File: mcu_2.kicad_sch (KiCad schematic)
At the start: 13 parts, among them U6 STM32G474RETx, Y3 Crystal 24MHz

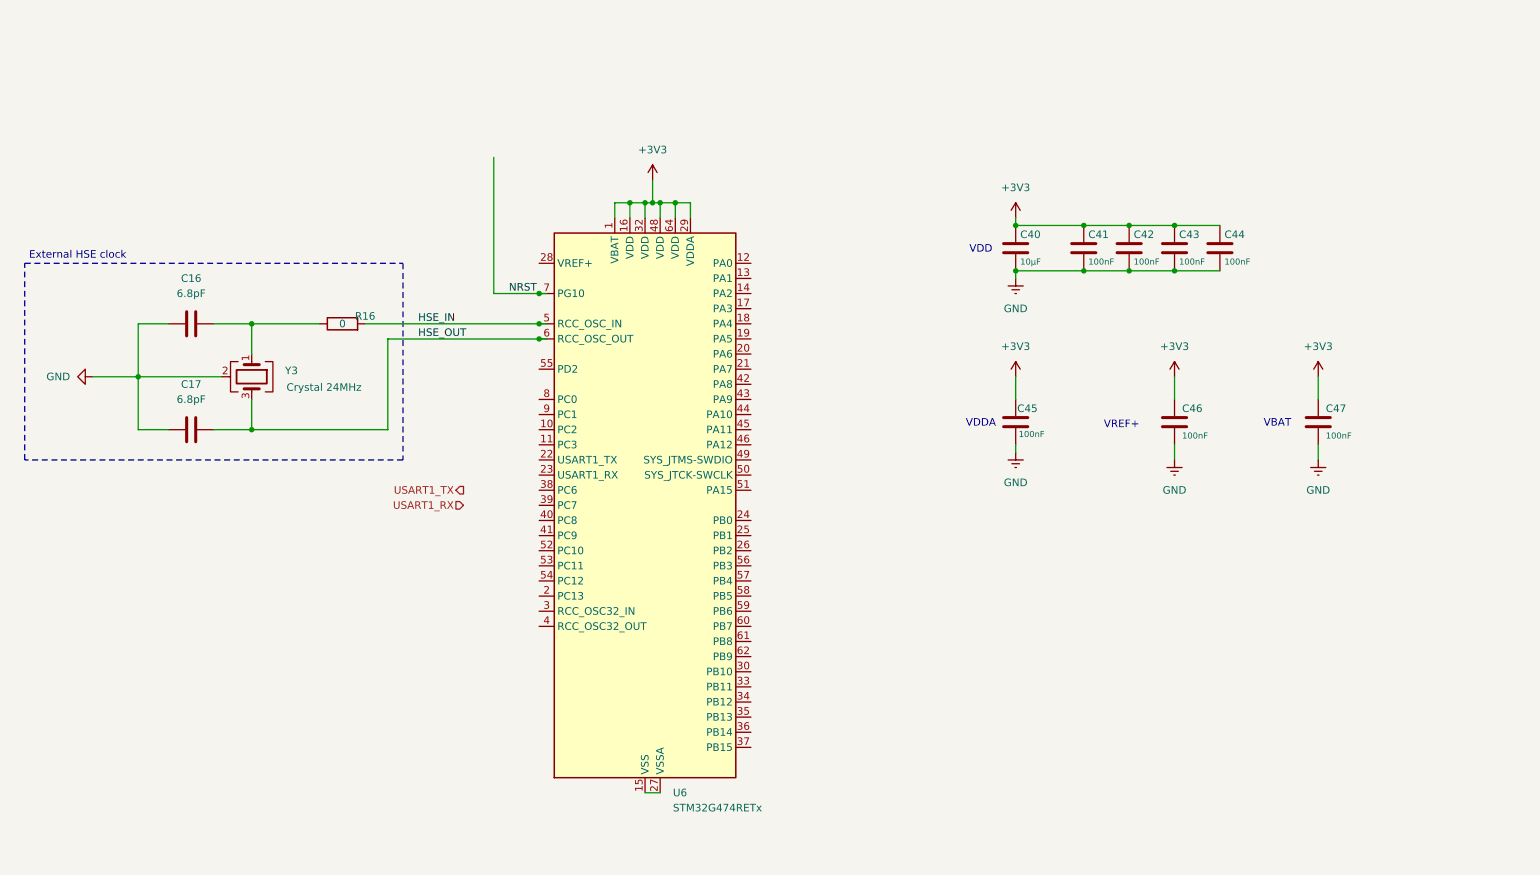
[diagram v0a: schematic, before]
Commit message: Generated scaffold for mcu2 finished brake sense rev2 finished adding second chip to nucleo devboard
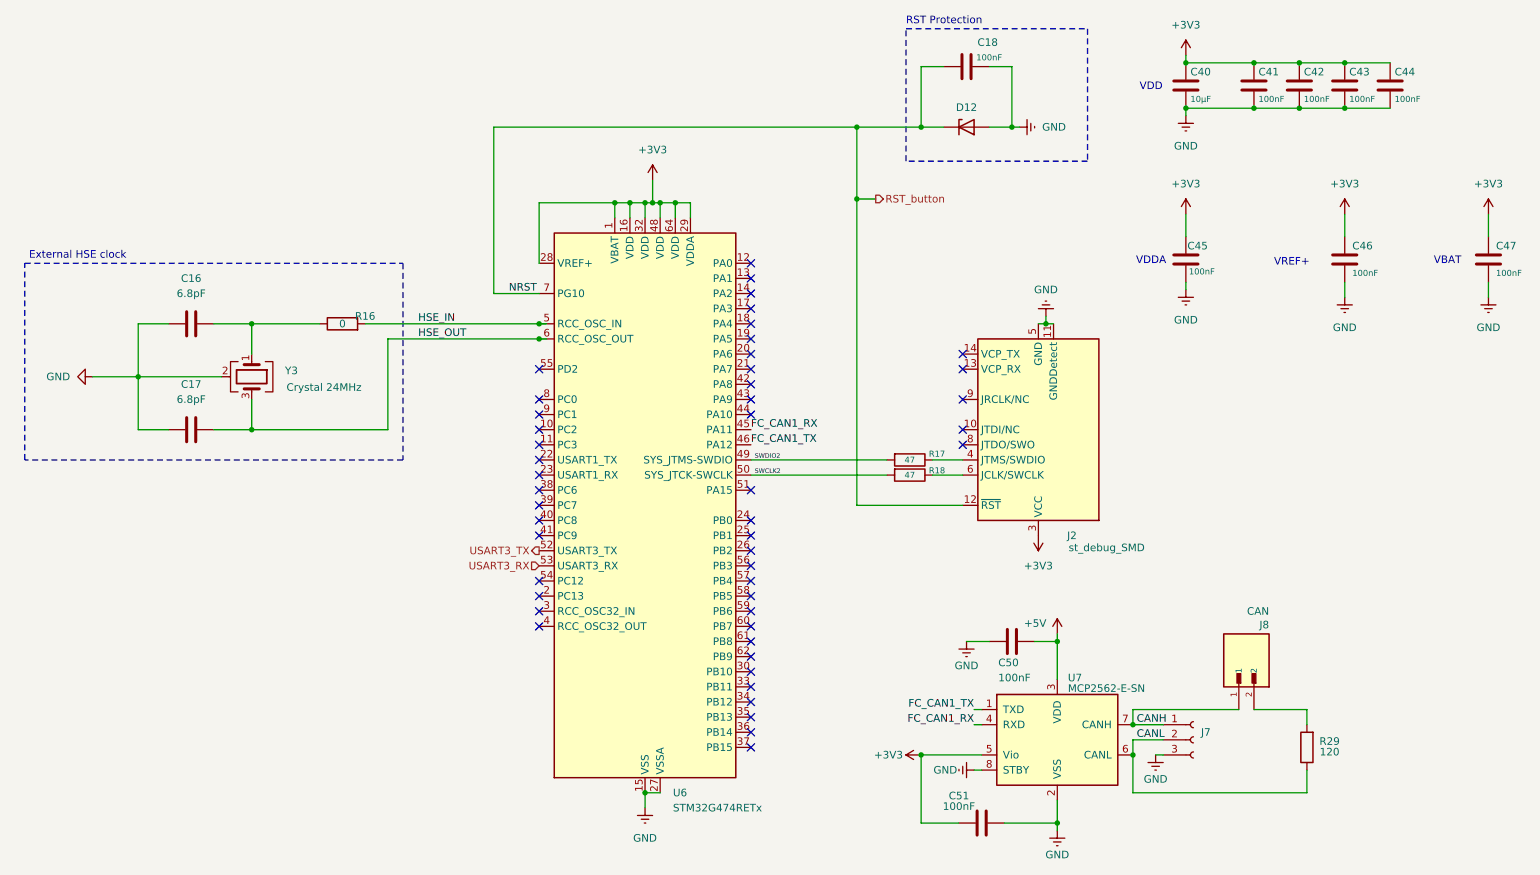
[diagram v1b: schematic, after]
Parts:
- added C18, C50, C51: 100nF, Capacitor_SMD:C_0603_1608Metric, symbol Device:C
- added D12: CDSOD323-T03, Diode_SMD:D_SOD-323, symbol Diode:PESD3V3U1UL
- added J2: st_debug_SMD, tinynav:PinHeader_2x07_P1.27mm_Vertical_SMD, symbol tinynav:st_debug_SMD
- added J7: Conn_01x03_Socket, tinynav:DF3-3P-2DSA, symbol Connector:Conn_01x03_Socket
- added J8: CAN, tinynav:HARWIN_M20-9990246, symbol tinynav:M20-9990246
- added R17, R18: 47, Resistor_SMD:R_0805_2012Metric, symbol Device:R
- added R29: 120, Resistor_SMD:R_0805_2012Metric, symbol Device:R
- added U7: MCP2562-E-SN, Package_SO:SOIC-8_3.9x4.9mm_P1.27mm, symbol Interface_CAN_LIN:MCP2562-E-SN
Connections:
- net +3V3: now also U6.28 (VREF+), C51.1, J2.3 (VCC), U7.5 (Vio)
- net GND: now also U6.15 (VSS), U6.27 (VSSA), U6.31 (VSS), U6.47 (VSS), U6.63 (VSS), C18.2, C50.1, C51.2, D12.2 (A), J2.11 (GNDDetect), J2.5 (GND), J2.7 (GND), J7.3 (Pin_3), U7.2 (VSS), U7.8 (STBY)
- net FC_CAN1_RX: now reaches U6.45 (PA11)
- net FC_CAN1_RX: now also U7.4 (RXD)
- net FC_CAN1_TX: now reaches U6.46 (PA12)
- net FC_CAN1_TX: now also U7.1 (TXD)
- net SWDIO2: now reaches U6.49 (PA13)
- net SWDIO2: now also R17.2
- net SWCLK2: now reaches U6.50 (PA14)
- net SWCLK2: now also R18.2
- net USART3_TX: now reaches U6.52 (PC10)
- net USART3_RX: now reaches U6.53 (PC11)
- net NRST renamed RST_button
- net RST_button: now also C18.1, D12.1 (K), J2.12 (~{RST})
- new net: J8.2, R29.2
- new net: J2.6 (JCLK/SWCLK), R18.1
- new net: J2.4 (JTMS/SWDIO), R17.1
- new net +5V: C50.2, U7.3 (VDD)
- new net CANH: J7.1 (Pin_1), J8.1, U7.7 (CANH)
- new net CANL: J7.2 (Pin_2), R29.1, U7.6 (CANL)
- no-connect marks 0 -> 48
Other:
- note added: "RST Protection"
- moved on the sheet: C40, C41, C42, C43, C44, C45, C46, C47

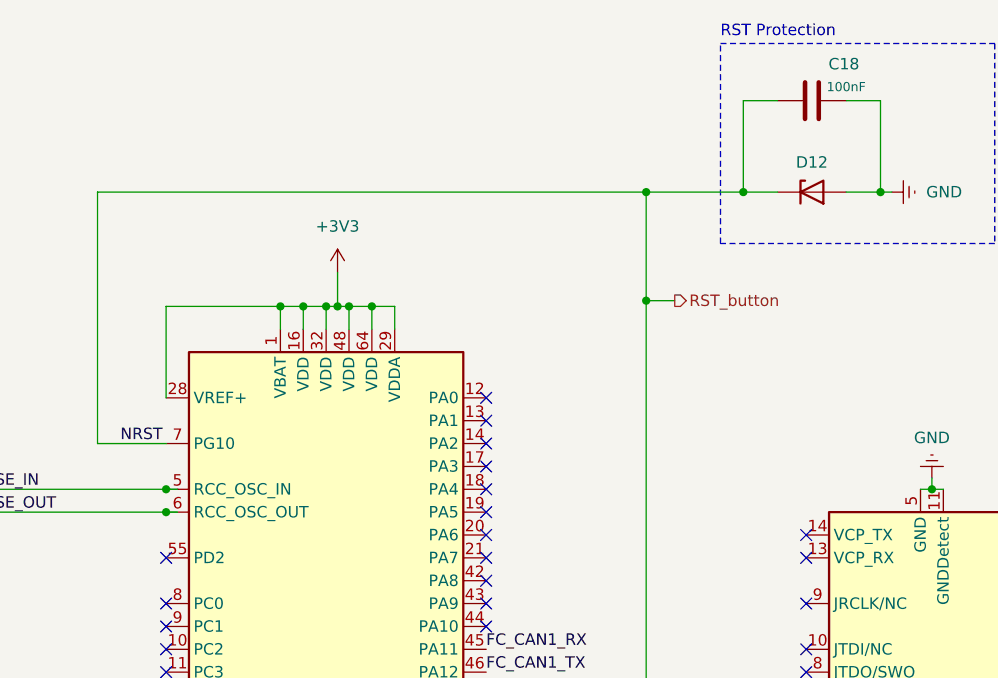
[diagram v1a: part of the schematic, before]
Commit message: Finished last thouches on brake sense and nucleo pcb (Ordered pcbs)
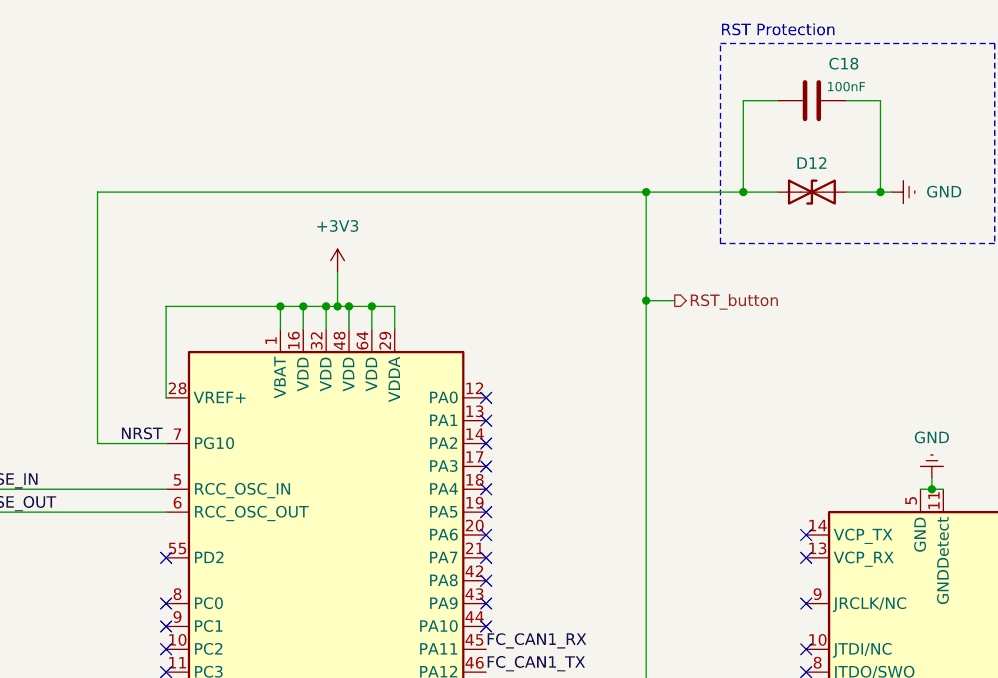
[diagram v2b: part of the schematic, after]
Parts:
- removed D12: CDSOD323-T03, Diode_SMD:D_SOD-323, symbol Diode:PESD3V3U1UL
- added D12: STS321033B401, Diode_SMD:D_SOD-323, symbol Device:D_TVS
- R17, R18: footprint Resistor_SMD:R_0805_2012Metric -> Resistor_SMD:R_0603_1608Metric
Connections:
- net GND: now also D12.2 (A2)
- net RST_button: now also D12.1 (A1)
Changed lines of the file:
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@@
 	)
 	(junction
-		(at 115.57 69.85)
-		(diameter 0)
-		(color 0 0 0 0)
-	)
-	(junction
 		(at 138.43 46.99)
 		(diameter 0)
@@
 	)
 	(junction
-		(at 115.57 67.31)
-		(diameter 0)
-		(color 0 0 0 0)
-	)
-	(junction
 		(at 202.565 120.65)
 		(diameter 0)
@@
 	(wire
 		(pts
+			(xy 90.17 69.85) (xy 115.57 69.85)
+		)
+		(stroke
+			(width 0)
+			(type default)
+		)
+	)
+	(wire
+		(pts
 			(xy 250.825 31.115) (xy 258.445 31.115)
 		)
@@
 	(wire
 		(pts
-			(xy 115.57 67.31) (xy 116.84 67.31)
-		)
-		(stroke
-			(width 0)
-			(type default)
-		)
-	)
-	(wire
-		(pts
 			(xy 202.565 151.13) (xy 202.565 152.4)
 		)
@@
 	(wire
 		(pts
-			(xy 90.17 69.85) (xy 115.57 69.85)
-		)
-		(stroke
-			(width 0)
-			(type default)
-		)
-	)
-	(wire
-		(pts
 			(xy 134.62 43.18) (xy 134.62 46.99)
 		)
@@
 	(wire
 		(pts
-			(xy 115.57 69.85) (xy 116.84 69.85)
+			(xy 224.155 32.385) (xy 224.155 31.115)
 		)
 		(stroke
@@
 	(wire
 		(pts
-			(xy 224.155 32.385) (xy 224.155 31.115)
+			(xy 128.27 46.99) (xy 130.81 46.99)
 		)
 		(stroke
@@
 	(wire
 		(pts
-			(xy 128.27 46.99) (xy 130.81 46.99)
+			(xy 183.515 24.13) (xy 179.705 24.13)
 		)
 		(stroke
@@
 	(wire
 		(pts
-			(xy 183.515 24.13) (xy 179.705 24.13)
+			(xy 115.57 57.15) (xy 115.57 46.99)
 		)
 		(stroke
@@
 	(wire
 		(pts
-			(xy 115.57 57.15) (xy 115.57 46.99)
+			(xy 86.36 67.31) (xy 115.57 67.31)
 		)
 		(stroke
@@
 	(wire
 		(pts
-			(xy 86.36 67.31) (xy 115.57 67.31)
-		)
-		(stroke
-			(width 0)
-			(type default)
-		)
-	)
-	(wire
-		(pts
 			(xy 215.265 137.16) (xy 220.345 137.16)
 		)
@@
 			)
 		)
-		(property "Footprint" "Resistor_SMD:R_0805_2012Metric"
+		(property "Footprint" "Resistor_SMD:R_0603_1608Metric"
 			(at 177.8 90.932 90)
 			(hide yes)
@@
 	)
 	(symbol
-		(lib_id "Diode:PESD3V3U1UL")
-		(at 187.325 34.29 0)
-		(unit 1)
-		(body_style 1)
-		(exclude_from_sim no)
-		(in_bom yes)
-		(on_board yes)
-		(in_pos_files yes)
-		(dnp no)
-		(property "Reference" "D12"
-			(at 187.325 30.988 0)
-			(show_name no)
-			(do_not_autoplace no)
-			(effects
-				(font
-					(size 1.27 1.27)
-				)
-			)
-		)
-		(property "Value" "CDSOD323-T03"
-			(at 187.579 32.004 0)
-			(hide yes)
-			(show_name no)
-			(do_not_autoplace no)
-			(effects
-				(font
-					(size 1.27 1.27)
-				)
-			)
-		)
-		(property "Footprint" "Diode_SMD:D_SOD-323"
-			(at 187.325 39.37 0)
-			(hide yes)
-			(show_name no)
-			(do_not_autoplace no)
-			(effects
-				(font
-					(size 1.27 1.27)
-				)
-			)
-		)
-		(property "Datasheet" ""
-			(at 187.325 29.21 0)
-			(hide yes)
-			(show_name no)
-			(do_not_autoplace no)
-			(effects
-				(font
-					(size 1.27 1.27)
-				)
-			)
-		)
-		(property "Description" ""
-			(at 187.325 26.67 0)
-			(hide yes)
-			(show_name no)
-			(do_not_autoplace no)
-			(effects
-				(font
-					(size 1.27 1.27)
-				)
-			)
-		)
-		(property "Sim.Pins" ""
-			(at 187.325 34.29 0)
-			(hide yes)
-			(show_name no)
-			(do_not_autoplace no)
-			(effects
-				(font
-					(size 1.27 1.27)
-				)
-			)
-		)
-		(pin "1"
-		)
-		(pin "2"
-		)
-		(instances
-			(project "Nucleo_devboard"
-				(path "/4250c3cc-f8c5-441a-9e80-e89bb6ada756/baf5d7d0-ff4f-4de6-b130-7faf308e626b"
-					(reference "D12")
-					(unit 1)
-				)
-			)
-		)
-	)
-	(symbol
 		(lib_id "power:GNDREF")
 		(at 202.565 152.4 0)
@@
 	)
 	(symbol
+		(lib_id "Device:D_TVS")
+		(at 187.325 34.29 0)
+		(unit 1)
+		(body_style 1)
+		(exclude_from_sim no)
+		(in_bom yes)
+		(on_board yes)
+		(in_pos_files yes)
+		(dnp no)
+		(property "Reference" "D12"
+			(at 187.325 31.115 0)
+			(show_name no)
+			(do_not_autoplace no)
+			(effects
+				(font
+					(size 1.27 1.27)
+				)
+			)
+		)
+		(property "Value" "STS321033B401"
+			(at 187.325 31.115 0)
+			(hide yes)
+			(show_name no)
+			(do_not_autoplace no)
+			(effects
+				(font
+					(size 1.27 1.27)
+				)
+			)
+		)
+		(property "Footprint" "Diode_SMD:D_SOD-323"
+			(at 187.325 34.29 0)
+			(hide yes)
+			(show_name no)
+			(do_not_autoplace no)
+			(effects
+				(font
+					(size 1.27 1.27)
+				)
+			)
+		)
+		(property "Datasheet" "https://www.eaton.com/content/dam/eaton/products/electronic-components/resources/data-sheet/eaton-sts321xxxbxx1-tvs-diode-esd-suppressor-data-sheet.pdf"
+			(at 187.325 34.29 0)
+			(hide yes)
+			(show_name no)
+			(do_not_autoplace no)
+			(effects
+				(font
+					(size 1.27 1.27)
+				)
+			)
+		)
+		(property "Description" "Bidirectional transient-voltage-suppression diode"
+			(at 187.325 34.29 0)
+			(hide yes)
+			(show_name no)
+			(do_not_autoplace no)
+			(effects
+				(font
+					(size 1.27 1.27)
+				)
+			)
+		)
+		(pin "1"
+		)
+		(pin "2"
+		)
+		(instances
+			(project "Nucleo_devboard"
+				(path "/4250c3cc-f8c5-441a-9e80-e89bb6ada756/baf5d7d0-ff4f-4de6-b130-7faf308e626b"
+					(reference "D12")
+					(unit 1)
+				)
+			)
+		)
+	)
+	(symbol
 		(lib_id "Device:R")
 		(at 177.8 90.17 270)
@@
 			)
 		)
-		(property "Footprint" "Resistor_SMD:R_0805_2012Metric"
+		(property "Footprint" "Resistor_SMD:R_0603_1608Metric"
 			(at 177.8 88.392 90)
 			(hide yes)

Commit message: volvo_h2 revision Revised switch regulator layout/components Changed brake circuit to use current sense amplifier Defined nets and nettclass constraints. Revises trace layout to fit new constraints.
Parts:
- J8: footprint tinynav:HARWIN_M20-9990246 -> tinynav:jumper_header; symbol tinynav:M20-9990246 -> tinynav:jumper_header
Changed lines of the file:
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@@
 	)
 	(symbol
-		(lib_id "tinynav:M20-9990246")
+		(lib_id "tinynav:jumper_header")
 		(at 235.585 124.46 90)
 		(unit 1)
@@
 			)
 		)
-		(property "Footprint" "tinynav:HARWIN_M20-9990246"
+		(property "Footprint" "tinynav:jumper_header"
 			(at 235.585 124.46 0)
 			(hide yes)
